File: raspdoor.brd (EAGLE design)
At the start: 92.4 x 47 mm, 44 parts, among them IC1 ATMEGA168-PU, IC2 ENC28J60SP, J1 1X2-3.5MM, J2 1X2-3.5MM, J3 1X2-3.5MM, J4 1X2-3.5MM, J5 1X2-3.5MM, Q2 MOSFET-NCHANNELFQP30N06L

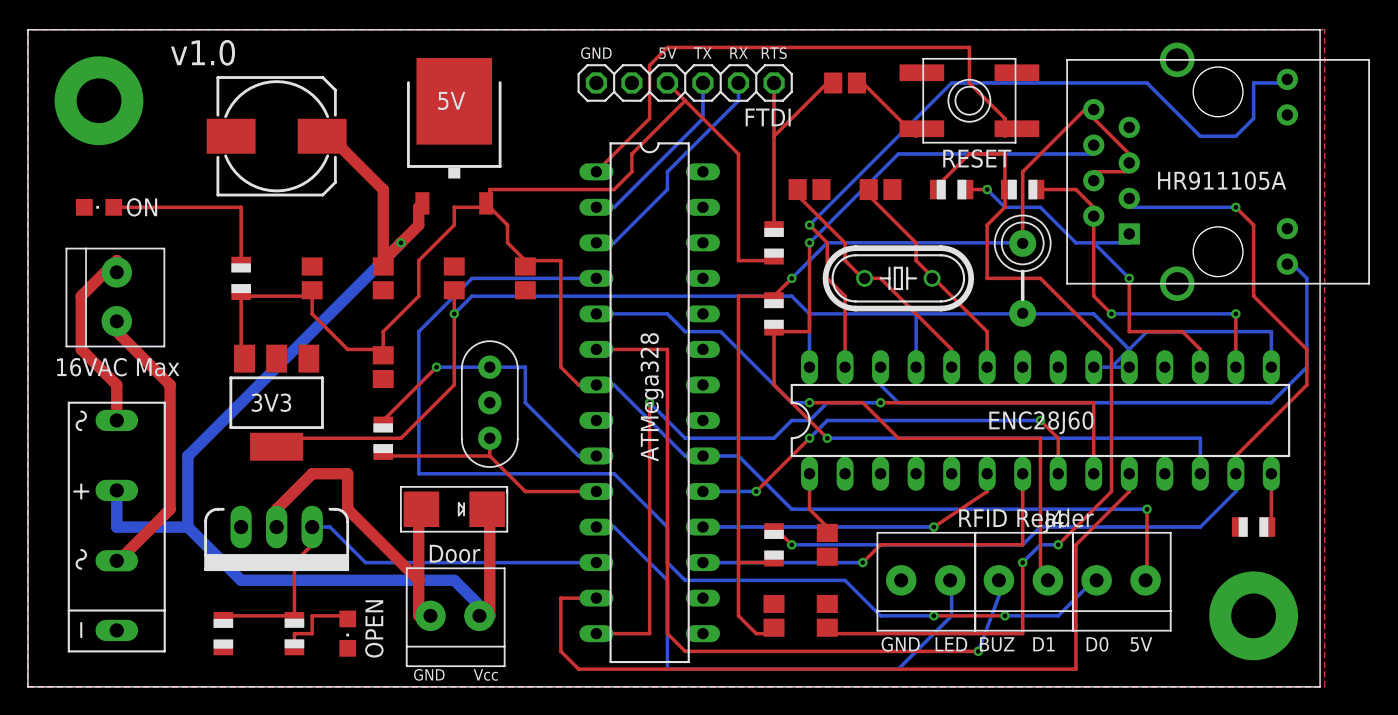
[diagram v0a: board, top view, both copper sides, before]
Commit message: Added an override button to schematic and PCB.
Allows for the hookup of a switch that will override RFID and cause
action in code immediately.
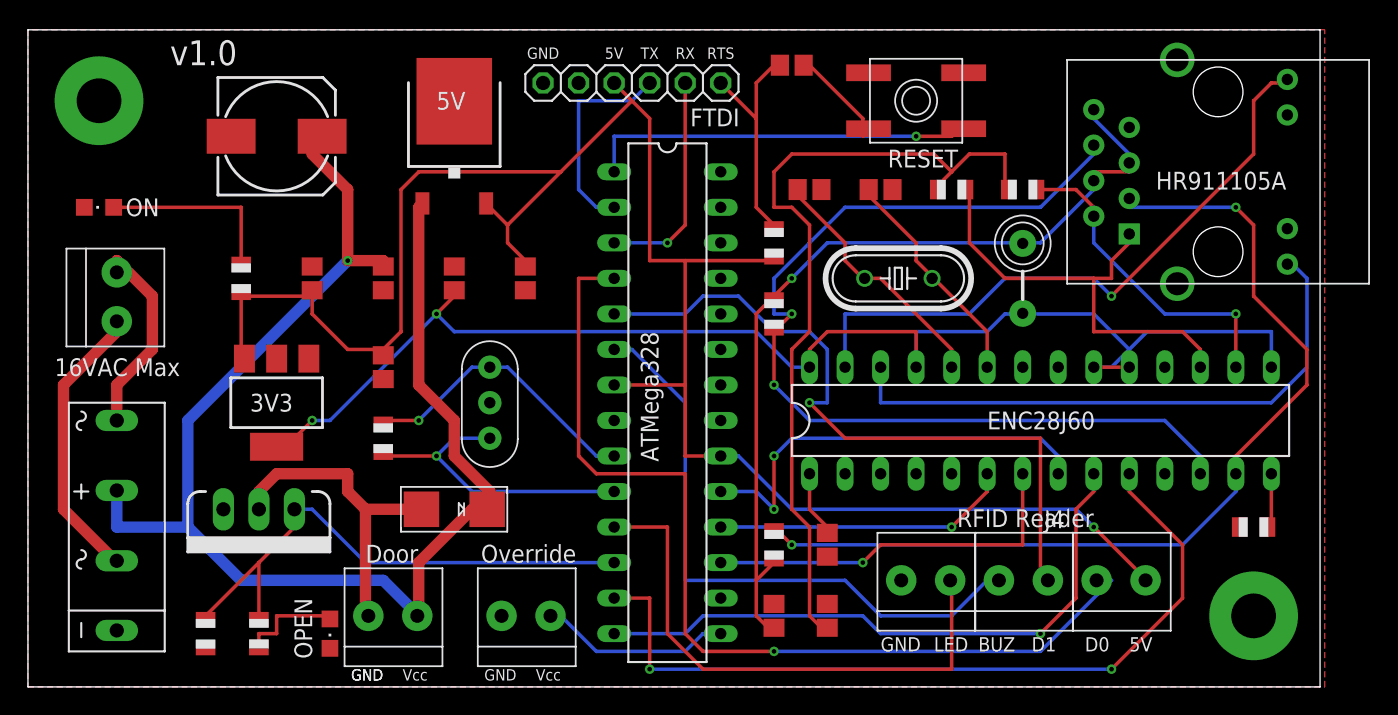
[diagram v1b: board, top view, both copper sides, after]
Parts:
- added J6: 1X2-3.5MM, adafruit:1X2-3.5MM
- moved J2 4.45 mm to (26.0, 5.08)
- moved C7 4.02 mm to (54.6, 44.5)
- moved FTDI 3.81 mm to (43.2, 43.2)
- moved RESET 3.81 mm to (63.5, 41.9)
- moved R10 2.54 mm to (16.5, 3.81)
- moved Q2 1.80 mm to (16.5, 12.7)
- moved R8 1.27 mm to (12.7, 3.81)
- moved OPEN 1.27 mm to (21.6, 3.81)
- moved IC1 1.27 mm to (45.7, 20.3)
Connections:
- new net N$17: IC1.15, J6.1
- net GND: now also J6.2
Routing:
- net CS: track 59.3 -> 44.5 mm, vias 2 -> 1
- net VCC: track 84.5 -> 99.0 mm
- net N$17: track 0.00 -> 13.7 mm
- net N$1: track 41.0 -> 27.7 mm, vias 0 -> 1
- net D0: track 79.7 -> 69.0 mm, vias 2 -> 1
- net BUZZER: track 54.0 -> 43.9 mm, vias 1 -> 0
- net N$8: track 73.0 -> 63.3 mm
- net NET-LED-ACTIVITY: track 54.6 -> 46.0 mm
- net N$13: track 65.2 -> 59.8 mm, vias 2 -> 0
- net MOSFET: track 33.9 -> 39.0 mm
- net D1: track 46.1 -> 50.7 mm
- net N$6: track 17.8 -> 22.2 mm, vias 0 -> 1
- net TPOUT+: track 28.2 -> 32.2 mm, vias 2 -> 0
- net +5V: track 136.3 -> 139.0 mm
- net N$14: track 25.8 -> 23.0 mm
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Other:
- board text added: "Override"
